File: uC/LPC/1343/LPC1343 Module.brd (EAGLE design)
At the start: 25.4 x 25.4 mm, 36 parts, among them CN1 USBMINIB, Q1 MMBT2907A, U1 LPC1343FBD48, U3 MCP130T, X1 USB-MICROB, Y2 12MHz

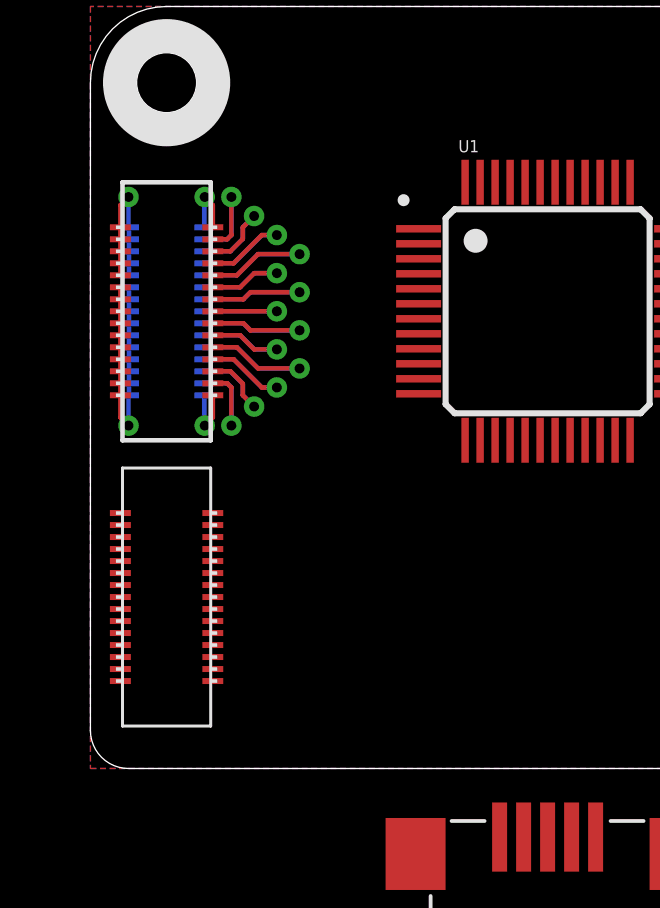
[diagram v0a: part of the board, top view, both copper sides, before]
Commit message: Updated Root1 header on LPC1343 MOdule
Signed-off-by: Cruz Monrreal II <Cruz.Monrreal@gmail.com>
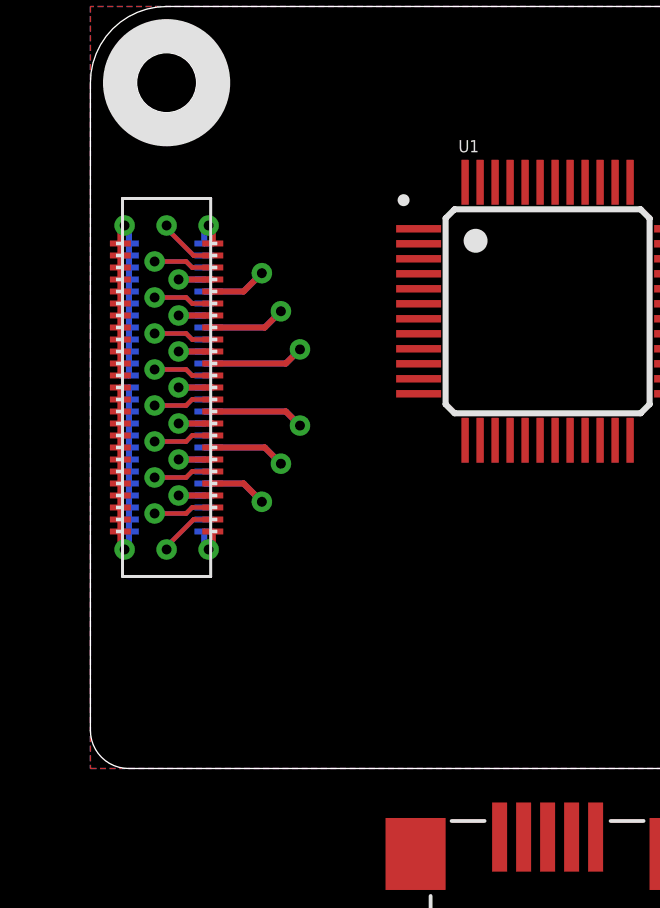
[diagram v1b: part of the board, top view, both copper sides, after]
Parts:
- removed U$9: DF40.30PIN.RECEPTACLE, hirose:DF40(XX)-30DS-0.4V
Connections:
- net 3.3V: now also U$8.3.3V@11, U$8.3.3V@12, U$8.3.3V@13, U$8.3.3V@14, U$8.3.3V@15, U$8.3.3V@16, U$8.3.3V@17, U$8.3.3V@18, U$8.3.3V@19, U$8.3.3V@20, U$8.3.3V@21, U$8.3.3V@22, U$8.3.3V@23, U$8.3.3V@24
- net GND: now also U$8.GND@21, U$8.GND@22, U$8.GND@23, U$8.GND@24, U$8.GND@25, U$8.GND@26
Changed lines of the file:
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@@
 <?xml version="1.0" encoding="utf-8"?>
 <!DOCTYPE eagle SYSTEM "eagle.dtd">
-<eagle version="6.1">
+<eagle version="6.3">
 <drawing>
 <settings>
@@
 <layers>
 <layer number="1" name="Top" color="4" fill="1" visible="yes" active="yes"/>
+<layer number="2" name="Route2" color="1" fill="3" visible="no" active="no"/>
+<layer number="3" name="Route3" color="4" fill="3" visible="no" active="no"/>
+<layer number="4" name="Route4" color="1" fill="4" visible="no" active="no"/>
+<layer number="5" name="Route5" color="4" fill="4" visible="no" active="no"/>
+<layer number="6" name="Route6" color="1" fill="8" visible="no" active="no"/>
+<layer number="7" name="Route7" color="4" fill="8" visible="no" active="no"/>
+<layer number="8" name="Route8" color="1" fill="2" visible="no" active="no"/>
+<layer number="9" name="Route9" color="4" fill="2" visible="no" active="no"/>
+<layer number="10" name="Route10" color="1" fill="7" visible="no" active="no"/>
+<layer number="11" name="Route11" color="4" fill="7" visible="no" active="no"/>
+<layer number="12" name="Route12" color="1" fill="5" visible="no" active="no"/>
+<layer number="13" name="Route13" color="4" fill="5" visible="no" active="no"/>
+<layer number="14" name="Route14" color="1" fill="6" visible="no" active="no"/>
+<layer number="15" name="Route15" color="4" fill="6" visible="no" active="no"/>
 <layer number="16" name="Bottom" color="1" fill="1" visible="yes" active="yes"/>
 <layer number="17" name="Pads" color="2" fill="1" visible="yes" active="yes"/>
@@
 </class>
 </classes>
-<designrules>
+<designrules name="default">
 <description language="de">&lt;b&gt;EAGLE Design Rules&lt;/b&gt;
 &lt;p&gt;
@@
 <element name="C11" library="microbuilder" package="0603" value="0.1µF" x="12.7" y="-28.575"/>
 <element name="R6" library="microbuilder" package="0603" value="1K" x="21.59" y="-36.83"/>
-<element name="U$9" library="hirose" package="DF40(XX)-30DS-0.4V" value="DF40.30PIN.RECEPTACLE" x="2.54" y="5.715" rot="R90"/>
 <element name="X1" library="SparkFun" package="USB-MICROB" value="USB-MICROB" x="29.21" y="19.685" rot="R90"/>
 </elements>
@@
 <wire x1="16.04" y1="-2.286" x2="16.84" y2="-2.286" width="0" layer="19" extent="1-1"/>
 <wire x1="10.94" y1="15.99" x2="16.04" y2="-2.286" width="0" layer="19" extent="1-1"/>
+<contactref element="U$8" pad="GND@21"/>
+<contactref element="U$8" pad="GND@22"/>
+<contactref element="U$8" pad="GND@23"/>
+<contactref element="U$8" pad="GND@24"/>
+<contactref element="U$8" pad="GND@25"/>
+<contactref element="U$8" pad="GND@26"/>
 </signal>
 <signal name="N$18">
@@
 <wire x1="10.94" y1="14.49" x2="13.65" y2="-25.13" width="0" layer="19" extent="1-1"/>
 <wire x1="14.49" y1="19.54" x2="10.94" y2="14.49" width="0" layer="19" extent="1-1"/>
-<wire x1="1.285" y1="16.44" x2="10.94" y2="14.49" width="0" layer="19" extent="1-16"/>
+<wire x1="1.285" y1="15.5" x2="10.94" y2="14.49" width="0" layer="19" extent="1-16"/>
+<contactref element="U$8" pad="3.3V@11"/>
+<contactref element="U$8" pad="3.3V@12"/>
+<contactref element="U$8" pad="3.3V@13"/>
+<contactref element="U$8" pad="3.3V@14"/>
+<contactref element="U$8" pad="3.3V@15"/>
+<contactref element="U$8" pad="3.3V@16"/>
+<contactref element="U$8" pad="3.3V@17"/>
+<contactref element="U$8" pad="3.3V@18"/>
+<contactref element="U$8" pad="3.3V@19"/>
+<contactref element="U$8" pad="3.3V@20"/>
+<contactref element="U$8" pad="3.3V@21"/>
+<contactref element="U$8" pad="3.3V@22"/>
+<contactref element="U$8" pad="3.3V@23"/>
+<contactref element="U$8" pad="3.3V@24"/>
 </signal>
 <signal name="N$1">
@@
 <contactref element="U$8" pad="WAKE"/>
 <contactref element="U1" pad="40"/>
-<wire x1="4.08" y1="12.44" x2="16.49" y2="19.54" width="0" layer="19" extent="1-1"/>
+<wire x1="3.795" y1="11.1" x2="16.49" y2="19.54" width="0" layer="19" extent="1-1"/>
 </signal>
 <signal name="RESET">
